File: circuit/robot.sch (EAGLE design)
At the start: 10 parts, among them M1 SERVO-FLIPPED, M2 SERVO-1, M3 SERVO-1, U1 ESP01

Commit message: second edition of the diy robot board with LM1117 vreg
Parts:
- IC1: device robot:V_REG_78XXTO-92 -> robot:V_REG_LM1117SOT223
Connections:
- net 3.3V: now also IC1.OUT@1
- net GND: now also IC1.ADJ; no longer IC1.GND

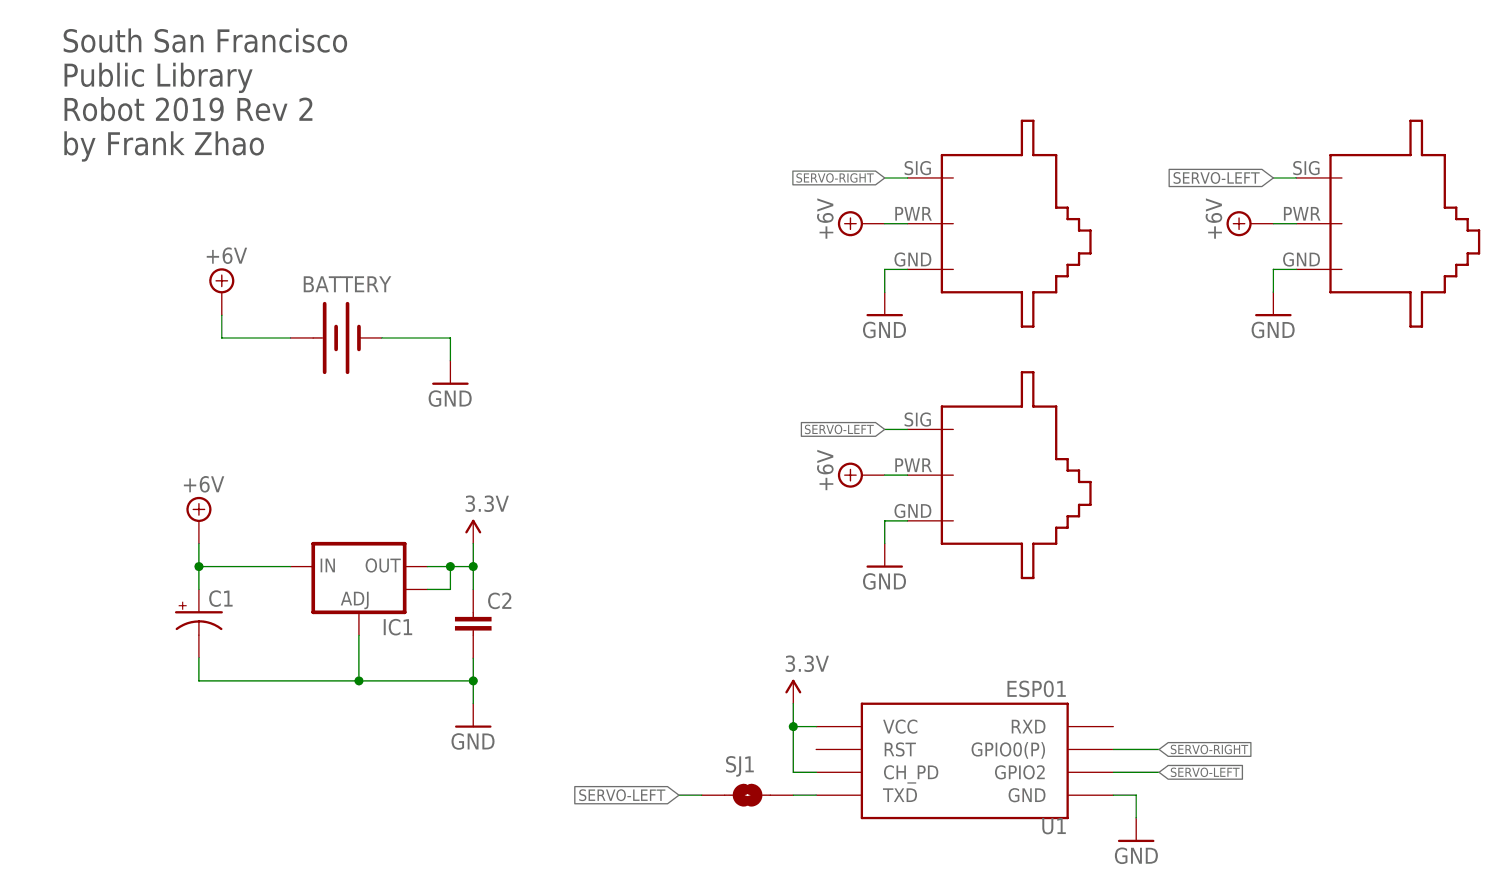
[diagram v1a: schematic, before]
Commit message: added Wemos based PCB
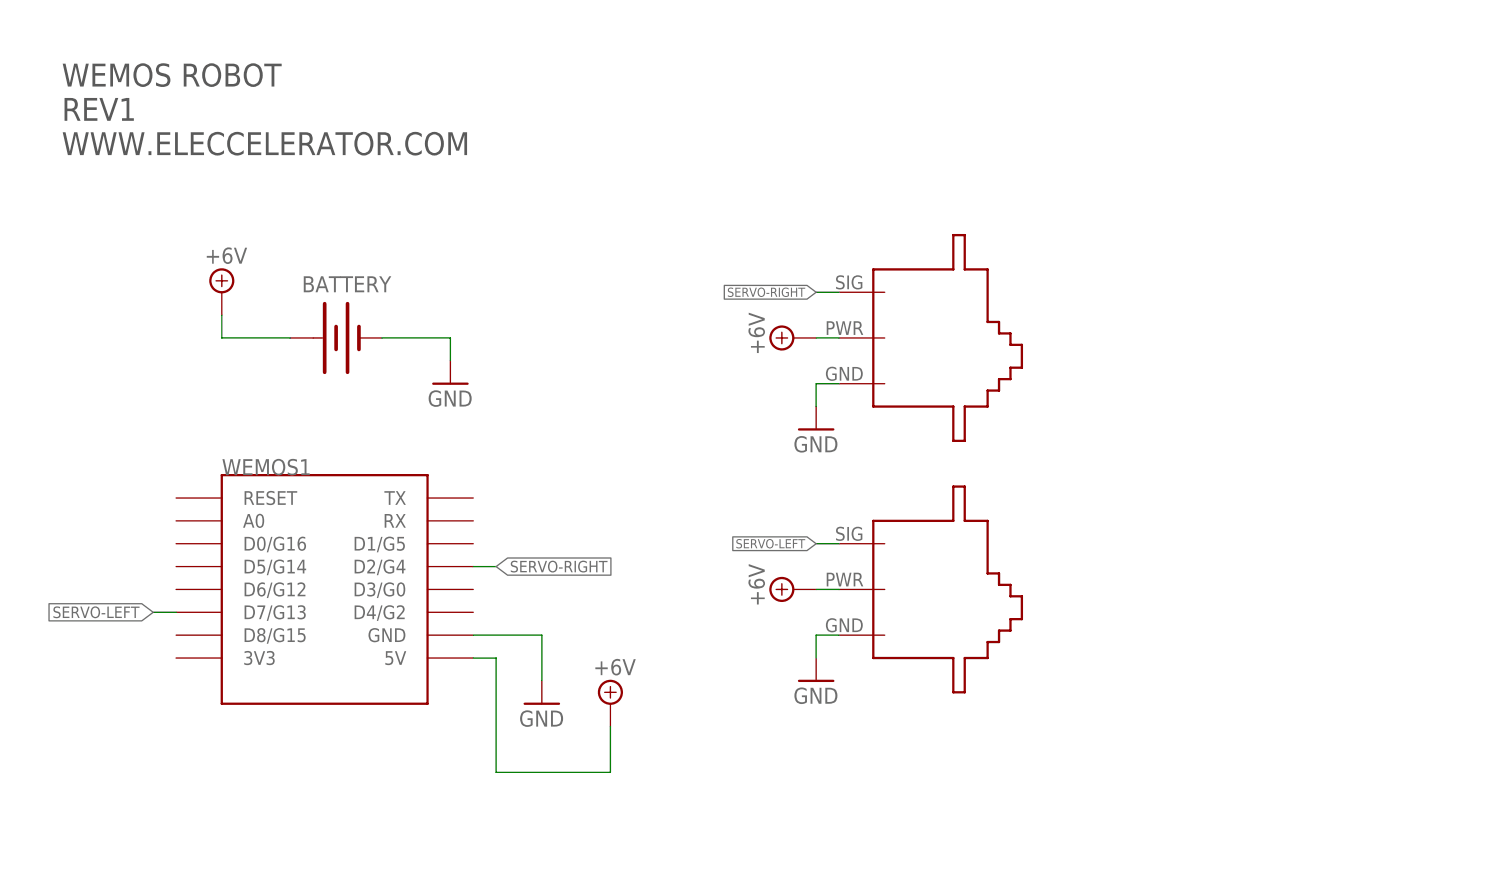
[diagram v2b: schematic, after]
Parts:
- removed C1: (no value), robot:CAP_POLPTH1
- removed C2: (no value), robot:CAPPTH
- removed IC1: (no value), robot:V_REG_LM1117SOT223
- removed M3: SERVO-1, robot:SERVO-1
- removed SJ1: SOLDERJUMPERNO, robot:SOLDERJUMPERNO
- removed U1: ESP01, robot:ESP01
- added U$1: HACKADAY-14MM, robot:HACKADAY-14MM
- added WEMOS1: (no value), robot:WEMOS-D1-MINI
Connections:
- removed net 3.3V: C2.1, IC1.OUT, IC1.OUT@1, U1.CH_PD, U1.VCC
- removed net N$1: SJ1.2, U1.TXD
- net +6V: now also WEMOS1.5V; no longer C1.+, IC1.IN, M3.PWR
- net GND: now also WEMOS1.GND; no longer C1.-, C2.2, IC1.ADJ, M3.GND, U1.GND
- net SERVO-LEFT: now also WEMOS1.D7/G13; no longer M3.SIG, SJ1.1, U1.GPIO2
- net SERVO-RIGHT: now also WEMOS1.D2/G4; no longer U1.GPIO0(P)
